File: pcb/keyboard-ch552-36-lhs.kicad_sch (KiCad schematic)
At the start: 55 parts, among them J1 PJ-320A, J1 USB Type-C Receptacle 12-pin, SW1 SW_SPST, SW2 SW_SPST, U1 CH552T

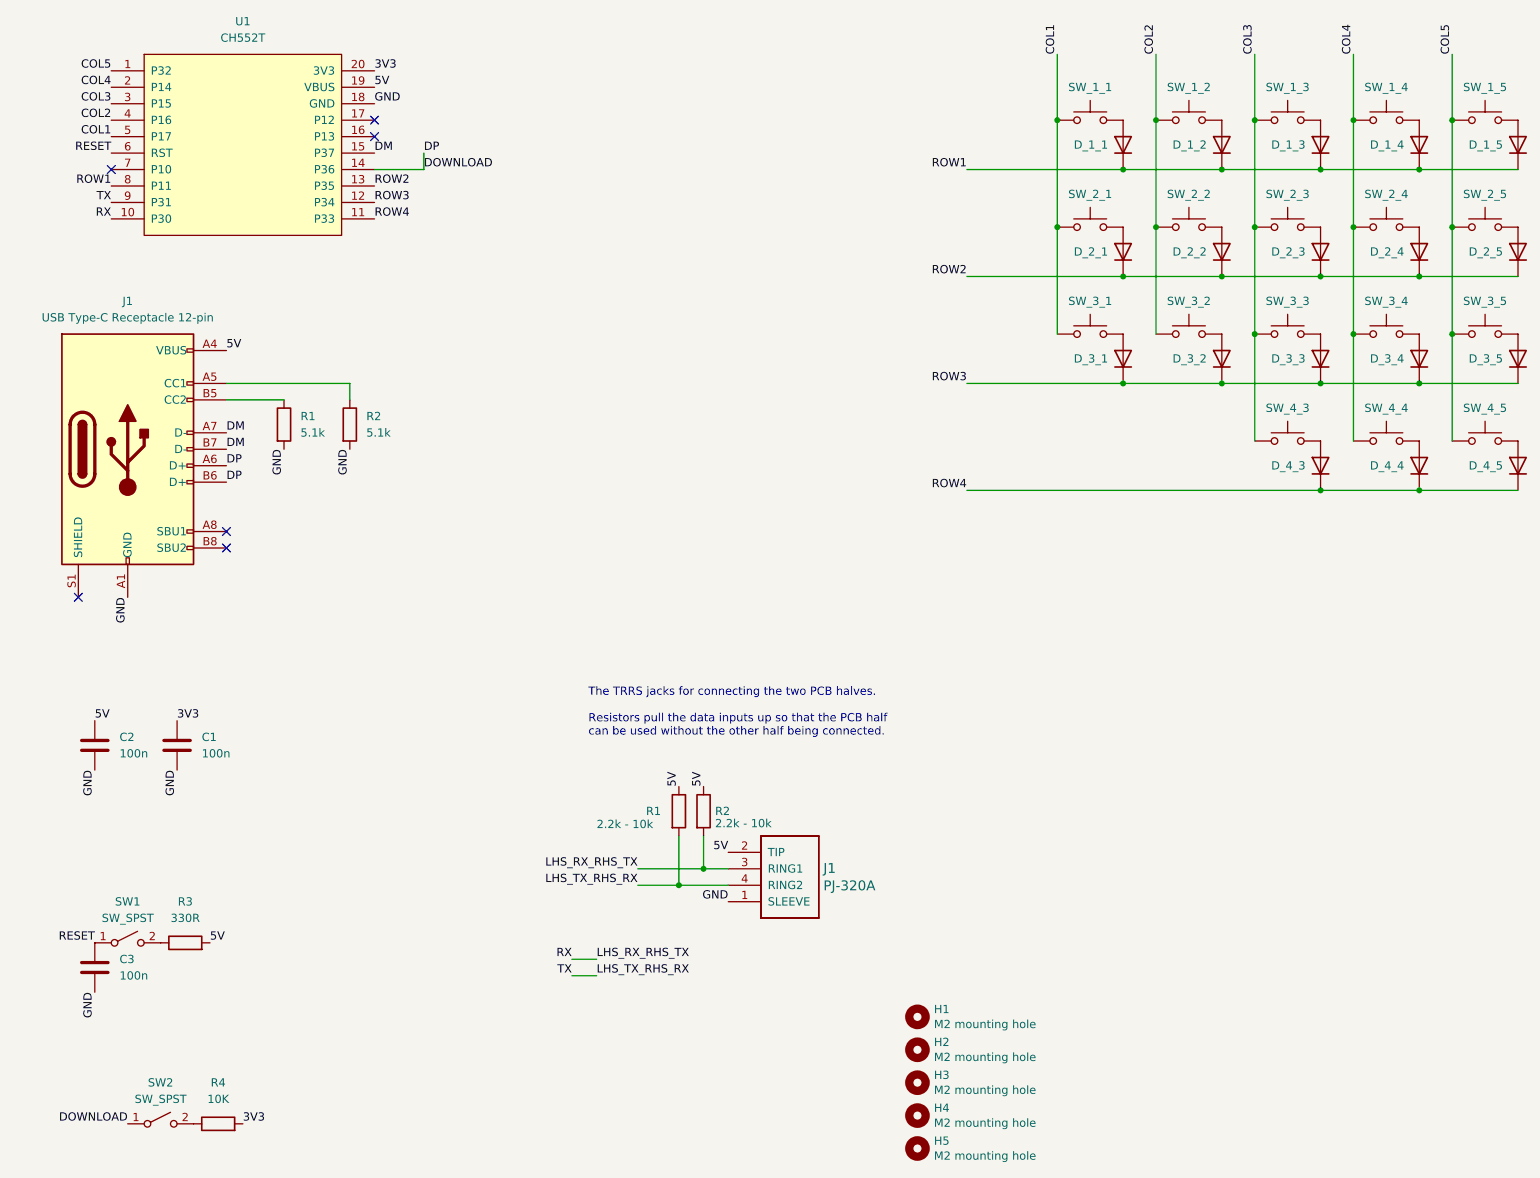
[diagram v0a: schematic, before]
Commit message: pcb: break out SPI pins for ISP flash on CH552-36 LHS
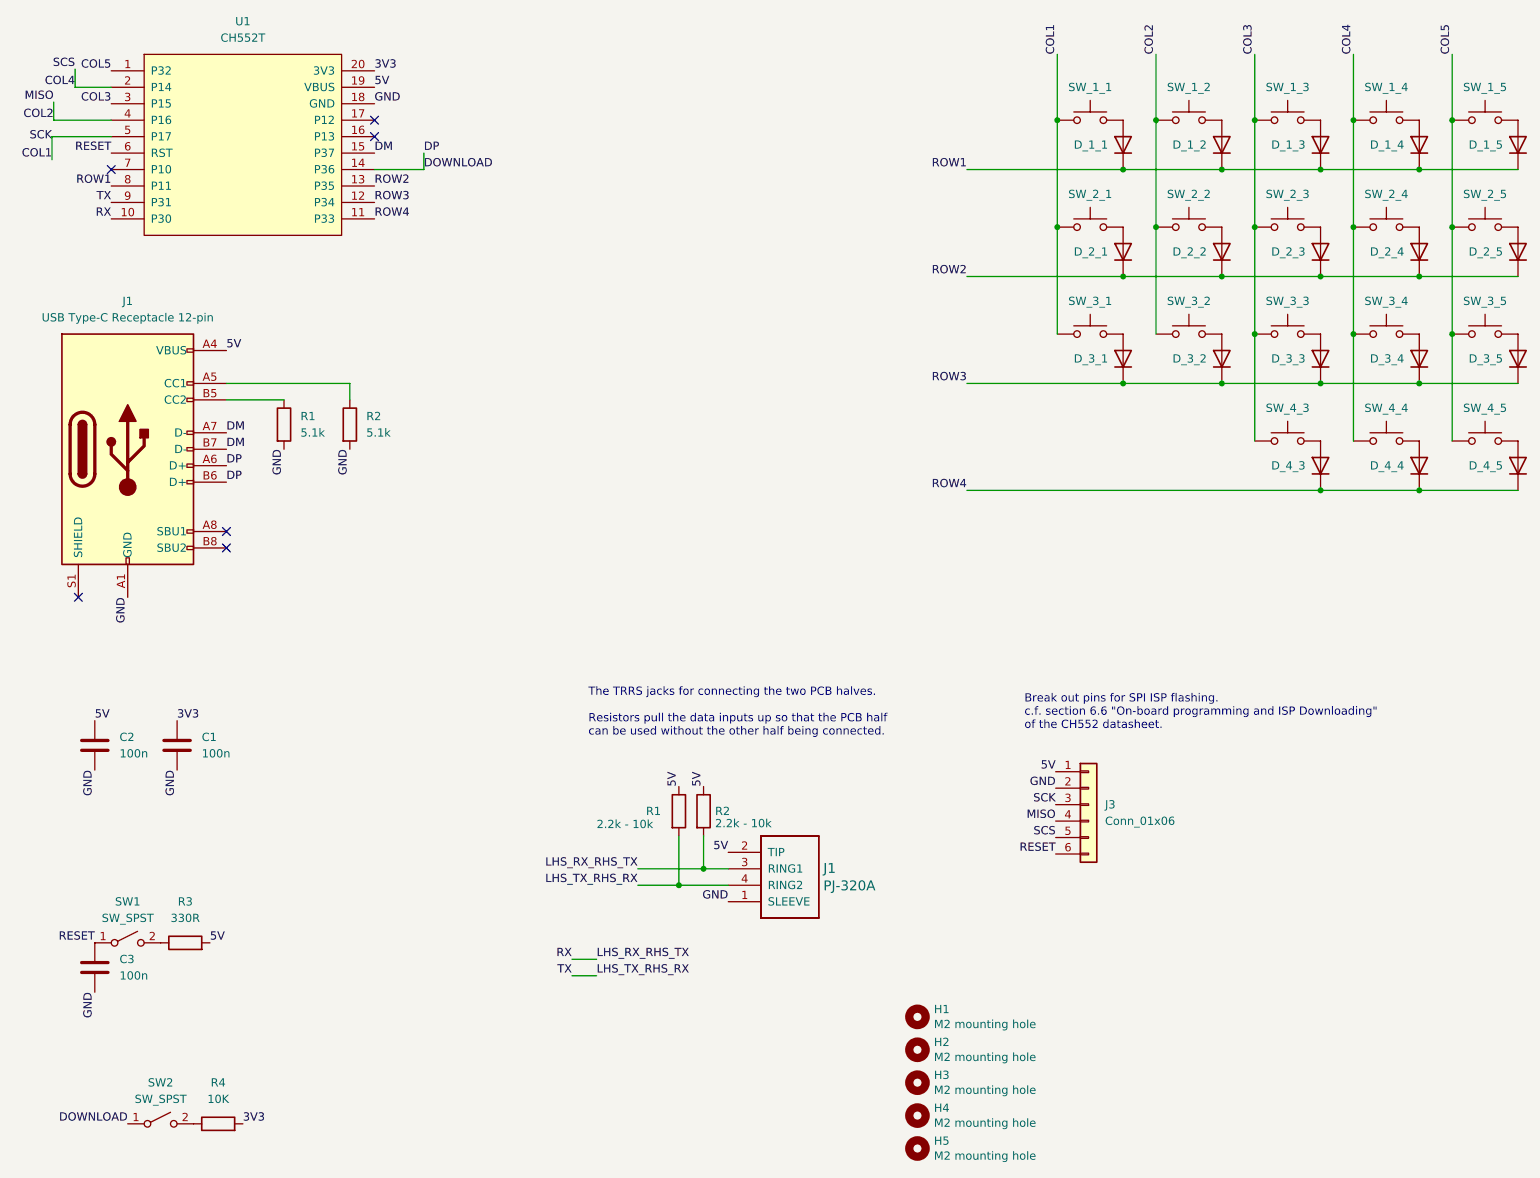
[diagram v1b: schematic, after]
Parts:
- added J3: Conn_01x06, symbol Connector_Generic:Conn_01x06
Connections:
- net 5V: now also J3.1 (Pin_1)
- net COL1: now also J3.3 (Pin_3)
- net COL2: now also J3.4 (Pin_4)
- net COL4: now also J3.5 (Pin_5)
- net GND: now also J3.2 (Pin_2)
- net RESET: now also J3.6 (Pin_6)
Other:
- note added: "Break out pins for SPI ISP flashing. c.f. section 6.6 "On-board programming and ISP Downloading" of the CH552 datasheet."
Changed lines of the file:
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@@
   (title_block
     (title "CH552-36 (LHS)")
-    (date "2023-12-16")
-    (rev "rev2023.1")
+    (date "2024-01-03")
+    (rev "rev2024.1-pre")
     (company "Richard Goulter (rgoulter)")
     (comment 1 "Using CH552T MCU.")
@@
     (stroke (width 0) (type default))
   )
+  (wire (pts (xy 22.606 34.29) (xy 31.75 34.29))
+    (stroke (width 0) (type default))
+  )
   (wire (pts (xy 208.28 31.75) (xy 208.28 48.26))
     (stroke (width 0) (type default))
@@
     (stroke (width 0) (type default))
   )
+  (wire (pts (xy 31.75 26.67) (xy 26.162 26.67))
+    (stroke (width 0) (type default))
+  )
   (wire (pts (xy 233.68 88.9) (xy 248.92 88.9))
     (stroke (width 0) (type default))
@@
     (stroke (width 0) (type default))
   )
+  (wire (pts (xy 22.606 37.846) (xy 22.606 34.29))
+    (stroke (width 0) (type default))
+  )
   (wire (pts (xy 208.28 48.26) (xy 208.28 64.77))
     (stroke (width 0) (type default))
@@
     (stroke (width 0) (type default))
   )
+  (wire (pts (xy 31.75 31.75) (xy 22.86 31.75))
+    (stroke (width 0) (type default))
+  )
+  (wire (pts (xy 22.86 28.956) (xy 22.86 31.75))
+    (stroke (width 0) (type default))
+  )
   (wire (pts (xy 223.52 48.26) (xy 223.52 64.77))
     (stroke (width 0) (type default))
@@
     (stroke (width 0) (type default))
   )
+  (wire (pts (xy 26.162 23.876) (xy 26.162 26.67))
+    (stroke (width 0) (type default))
+  )
   (wire (pts (xy 123.19 147.32) (xy 127 147.32))
     (stroke (width 0) (type default))
+  )
+  (text "Break out pins for SPI ISP flashing.\nc.f. section 6.6 \"On-board programming and ISP Downloading\"\nof the CH552 datasheet."
+    (at 172.72 125.984 0)
+    (effects (font (size 1.27 1.27)) (justify left bottom))
   )
   (text "The TRRS jacks for connecting the two PCB halves.\n\nResistors pull the data inputs up so that the PCB half\ncan be used without the other half being connected."
@@
     (effects (font (size 1.27 1.27)) (justify left bottom))
   )
+  (label "MISO" (at 177.546 139.954 180) (fields_autoplaced)
+    (effects (font (size 1.27 1.27)) (justify right bottom))
+  )
   (label "5V" (at 29.21 124.46 0) (fields_autoplaced)
     (effects (font (size 1.27 1.27)) (justify left bottom))
@@
     (effects (font (size 1.27 1.27)) (justify right bottom))
   )
-  (label "COL4" (at 31.75 26.67 180) (fields_autoplaced)
+  (label "RESET" (at 177.546 145.034 180) (fields_autoplaced)
+    (effects (font (size 1.27 1.27)) (justify right bottom))
+  )
+  (label "SCK" (at 22.606 35.052 180) (fields_autoplaced)
+    (effects (font (size 1.27 1.27)) (justify right bottom))
+  )
+  (label "COL4" (at 26.162 26.67 180) (fields_autoplaced)
     (effects (font (size 1.27 1.27)) (justify right bottom))
   )
@@
     (effects (font (size 1.27 1.27)) (justify left bottom))
   )
+  (label "5V" (at 177.546 132.334 180) (fields_autoplaced)
+    (effects (font (size 1.27 1.27)) (justify right bottom))
+  )
   (label "ROW4" (at 163.83 88.9 180) (fields_autoplaced)
     (effects (font (size 1.27 1.27)) (justify right bottom))
@@
     (effects (font (size 1.27 1.27)) (justify left bottom))
   )
+  (label "MISO" (at 22.86 28.956 180) (fields_autoplaced)
+    (effects (font (size 1.27 1.27)) (justify right bottom))
+  )
   (label "DP" (at 49.53 87.63 0) (fields_autoplaced)
     (effects (font (size 1.27 1.27)) (justify left bottom))
@@
     (effects (font (size 1.27 1.27)) (justify left bottom))
   )
-  (label "COL1" (at 31.75 34.29 180) (fields_autoplaced)
+  (label "COL1" (at 22.606 37.846 180) (fields_autoplaced)
     (effects (font (size 1.27 1.27)) (justify right bottom))
   )
@@
     (effects (font (size 1.27 1.27)) (justify left bottom))
   )
-  (label "COL2" (at 31.75 31.75 180) (fields_autoplaced)
+  (label "COL2" (at 22.86 31.75 180) (fields_autoplaced)
     (effects (font (size 1.27 1.27)) (justify right bottom))
   )
@@
     (effects (font (size 1.27 1.27)) (justify left bottom))
   )
+  (label "SCK" (at 177.546 137.414 180) (fields_autoplaced)
+    (effects (font (size 1.27 1.27)) (justify right bottom))
+  )
   (label "GND" (at 58.42 82.55 270) (fields_autoplaced)
     (effects (font (size 1.27 1.27)) (justify right bottom))
@@
     (effects (font (size 1.27 1.27)) (justify left bottom))
   )
+  (label "SCS" (at 26.162 23.876 180) (fields_autoplaced)
+    (effects (font (size 1.27 1.27)) (justify right bottom))
+  )
   (label "GND" (at 41.91 132.08 270) (fields_autoplaced)
     (effects (font (size 1.27 1.27)) (justify right bottom))
@@
     (effects (font (size 1.27 1.27)) (justify left bottom))
   )
+  (label "GND" (at 177.546 134.874 180) (fields_autoplaced)
+    (effects (font (size 1.27 1.27)) (justify right bottom))
+  )
   (label "5V" (at 72.39 26.67 0) (fields_autoplaced)
     (effects (font (size 1.27 1.27)) (justify left bottom))
@@
   )
   (label "DOWNLOAD" (at 34.29 186.69 180) (fields_autoplaced)
+    (effects (font (size 1.27 1.27)) (justify right bottom))
+  )
+  (label "SCS" (at 177.546 142.494 180) (fields_autoplaced)
     (effects (font (size 1.27 1.27)) (justify right bottom))
   )
@@
         )
       )
+    )
+  )
+  (symbol (lib_id "Connector_Generic:Conn_01x06") (at 182.626 137.414 0) (unit 1)
+    (in_bom yes) (on_board yes) (dnp no) (fields_autoplaced)
+    (property "Reference" "J3" (at 185.166 137.414 0)
+      (effects (font (size 1.27 1.27)) (justify left))
+    )
+    (property "Value" "Conn_01x06" (at 185.166 139.954 0)
+      (effects (font (size 1.27 1.27)) (justify left))
+    )
+    (property "Footprint" "" (at 182.626 137.414 0)
+      (effects (font (size 1.27 1.27)) hide)
+    )
+    (property "Datasheet" "~" (at 182.626 137.414 0)
+      (effects (font (size 1.27 1.27)) hide)
+    )
+    (pin "1")
+    (pin "2")
+    (pin "3")
+    (pin "4")
+    (pin "5")
+    (pin "6")
+    (instances
+      (project "keyboard-ch552-36-lhs"
+        (path "/491af640-c615-48ab-84d8-9b166bc1ab37"
+          (reference "J3") (unit 1)
+        )
+      )
